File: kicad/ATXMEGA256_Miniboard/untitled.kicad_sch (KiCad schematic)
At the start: 11 parts, among them U2 AMS1117-3.3

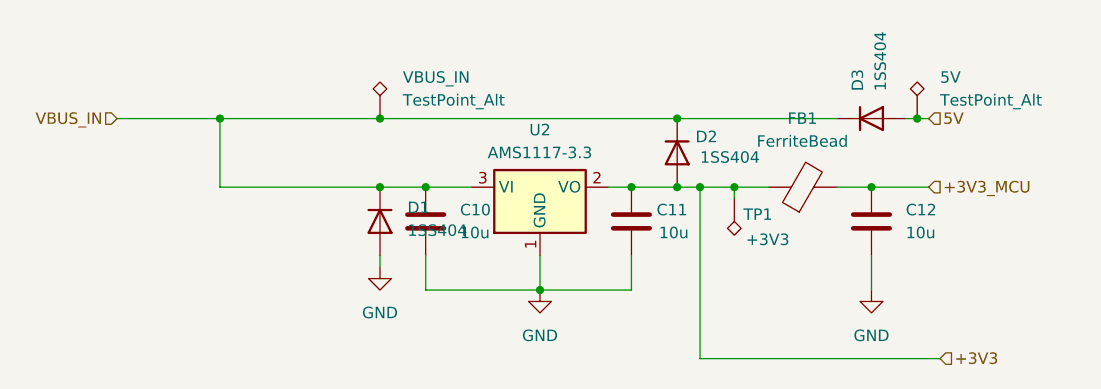
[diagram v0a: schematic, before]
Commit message: deleting flash module
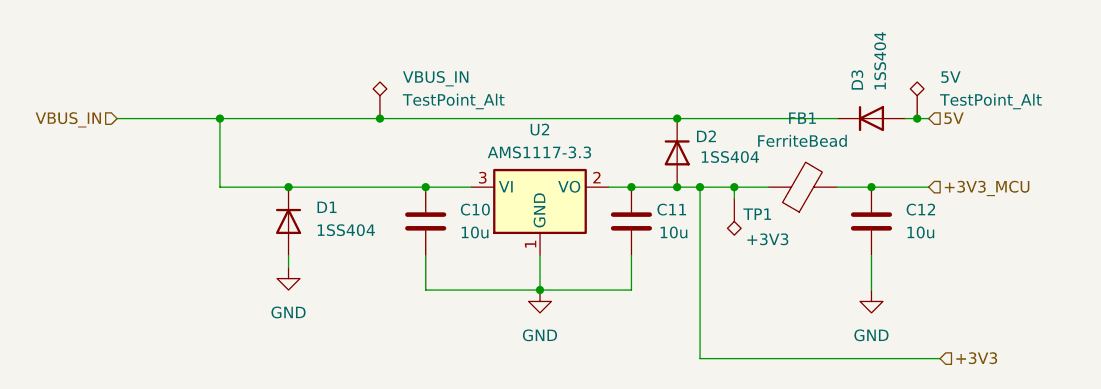
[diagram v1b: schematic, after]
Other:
- moved on the sheet: D1
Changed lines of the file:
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@@
-	)
-	(junction
-		(at 82.55 46.99)
-		(diameter 0)
-		(color 0 0 0 0)
 	)
 	(junction
@@
 	)
 	(junction
+		(at 72.39 46.99)
+		(diameter 0)
+		(color 0 0 0 0)
+	)
+	(junction
 		(at 87.63 46.99)
 		(diameter 0)
@@
 	(wire
 		(pts
+			(xy 72.39 46.99) (xy 87.63 46.99)
+		)
+		(stroke
+			(width 0)
+			(type default)
+		)
+	)
+	(wire
+		(pts
 			(xy 144.78 66.04) (xy 118.11 66.04)
 		)
@@
 	(wire
 		(pts
-			(xy 64.77 46.99) (xy 82.55 46.99)
+			(xy 64.77 46.99) (xy 72.39 46.99)
 		)
 		(stroke
@@
 	(wire
 		(pts
-			(xy 82.55 55.88) (xy 82.55 54.61)
+			(xy 72.39 55.88) (xy 72.39 54.61)
 		)
 		(stroke
@@
 		(pts
 			(xy 137.16 46.99) (xy 143.51 46.99)
-		)
-		(stroke
-			(width 0)
-			(type default)
-		)
-	)
-	(wire
-		(pts
-			(xy 82.55 46.99) (xy 87.63 46.99)
 		)
 		(stroke
@@
 	(symbol
 		(lib_id "Diode:1N4007")
-		(at 82.55 50.8 270)
+		(at 72.39 50.8 270)
 		(unit 1)
 		(exclude_from_sim no)
@@
 		(dnp no)
 		(property "Reference" "D1"
-			(at 85.598 49.276 90)
+			(at 75.438 49.276 90)
 			(effects
 				(font
@@
 		)
 		(property "Value" "1SS404"
-			(at 85.598 51.816 90)
+			(at 75.438 51.816 90)
 			(effects
 				(font
@@
 		)
 		(property "Footprint" "Diode_THT:D_DO-41_SOD81_P10.16mm_Horizontal"
-			(at 78.105 50.8 0)
+			(at 67.945 50.8 0)
 			(effects
 				(font
@@
 		)
 		(property "Datasheet" "http://www.vishay.com/docs/88503/1n4001.pdf"
-			(at 82.55 50.8 0)
+			(at 72.39 50.8 0)
 			(effects
 				(font
@@
 		)
 		(property "Description" "1000V 1A General Purpose Rectifier Diode, DO-41"
-			(at 82.55 50.8 0)
+			(at 72.39 50.8 0)
 			(effects
 				(font
@@
 		)
 		(property "Sim.Device" "D"
-			(at 82.55 50.8 0)
+			(at 72.39 50.8 0)
 			(effects
 				(font
@@
 		)
 		(property "Sim.Pins" "1=K 2=A"
-			(at 82.55 50.8 0)
+			(at 72.39 50.8 0)
 			(effects
 				(font
@@
 	(symbol
 		(lib_id "power:GND")
-		(at 82.55 55.88 0)
+		(at 72.39 55.88 0)
 		(unit 1)
 		(exclude_from_sim no)
@@
 		(fields_autoplaced yes)
 		(property "Reference" "#PWR06"
-			(at 82.55 62.23 0)
+			(at 72.39 62.23 0)
 			(effects
 				(font
@@
 		)
 		(property "Value" "GND"
-			(at 82.55 60.96 0)
+			(at 72.39 60.96 0)
 			(effects
 				(font
@@
 		)
 		(property "Footprint" ""
-			(at 82.55 55.88 0)
+			(at 72.39 55.88 0)
 			(effects
 				(font
@@
 		)
 		(property "Datasheet" ""
-			(at 82.55 55.88 0)
+			(at 72.39 55.88 0)
 			(effects
 				(font
@@
 		)
 		(property "Description" "Power symbol creates a global label with name \"GND\" , ground"
-			(at 82.55 55.88 0)
-			(effects
-				(font
+			(at 72.39 55.88 0)
+			(effects
+				(font
